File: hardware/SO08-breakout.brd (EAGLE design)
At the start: 12.4 x 20.3 mm, 3 parts, among them IC1 OPAMP-DUALU

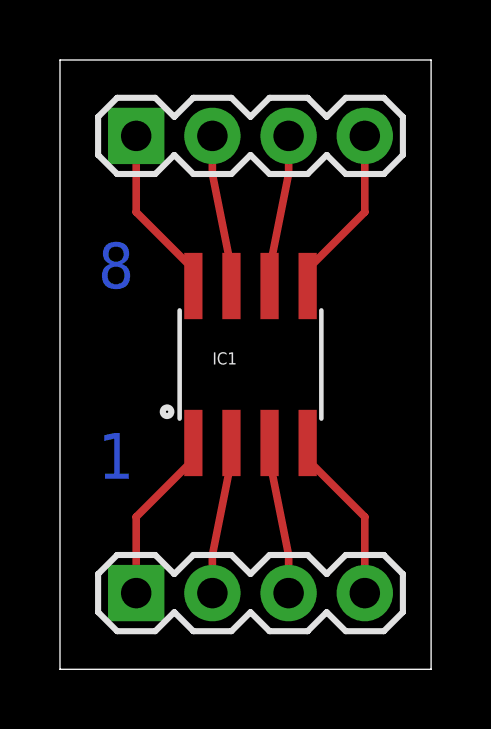
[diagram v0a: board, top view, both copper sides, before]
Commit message: made board a bit smaller
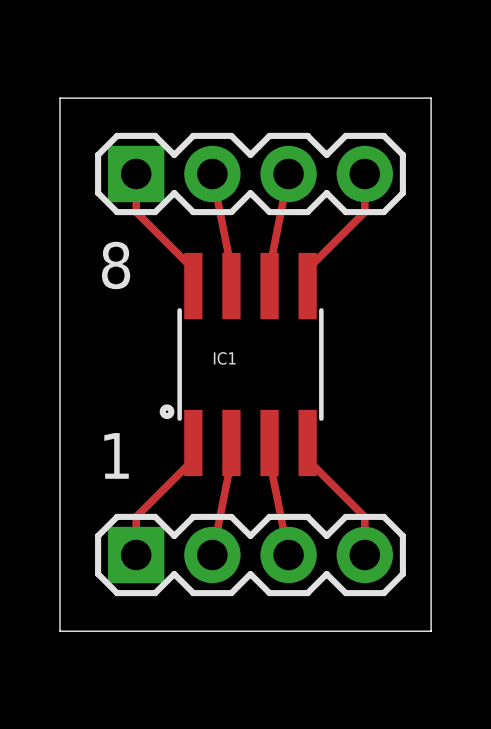
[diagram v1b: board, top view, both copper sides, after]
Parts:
- moved J1 1.27 mm to (2.54, 3.81)
- moved J2 1.27 mm to (2.54, 16.5)
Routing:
- net 3: track 5.07 -> 3.80 mm
- net 2: track 5.07 -> 3.80 mm
- net 1: track 5.79 -> 4.52 mm
- net 7: track 5.07 -> 3.80 mm
- net 6: track 5.07 -> 3.80 mm
- net 8: track 5.79 -> 4.52 mm
- net 5: track 5.79 -> 4.52 mm
- net 4: track 5.79 -> 4.52 mm
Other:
- board size 12.4 x 20.3 mm -> 12.4 x 17.8 mm
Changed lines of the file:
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@@
 <board>
 <plain>
-<wire x1="0" y1="0" x2="12.37" y2="0" width="0" layer="20"/>
-<wire x1="12.37" y1="0" x2="12.37" y2="20.31" width="0" layer="20"/>
-<wire x1="12.37" y1="20.31" x2="0" y2="20.31" width="0" layer="20"/>
-<wire x1="0" y1="20.31" x2="0" y2="0" width="0" layer="20"/>
-<text x="1.27" y="12.7" size="1.524" layer="16">8</text>
-<text x="1.27" y="6.35" size="1.524" layer="16">1</text>
+<wire x1="0" y1="1.27" x2="12.37" y2="1.27" width="0" layer="20"/>
+<wire x1="12.37" y1="1.27" x2="12.37" y2="19.04" width="0" layer="20"/>
+<wire x1="12.37" y1="19.04" x2="0" y2="19.04" width="0" layer="20"/>
+<wire x1="0" y1="19.04" x2="0" y2="1.27" width="0" layer="20"/>
+<text x="1.27" y="12.7" size="1.524" layer="121">8</text>
+<text x="1.27" y="6.35" size="1.524" layer="121">1</text>
 </plain>
 <attributes>
@@
 <elements>
 <element name="IC1" library="SparkFun-AnalogIC" package="SO08" value="OPAMP-DUALU" x="6.35" y="10.16"/>
-<element name="J1" library="SparkFun-Connectors" package="1X04" value="" x="2.54" y="2.54" smashed="yes">
-<attribute name="PROD_ID" value="CONN-09696" x="2.54" y="2.54" size="1.778" layer="27" display="off"/>
-<attribute name="VALUE" x="1.27" y="-0.635" size="1.27" layer="27"/>
+<element name="J1" library="SparkFun-Connectors" package="1X04" value="" x="2.54" y="3.81" smashed="yes">
+<attribute name="PROD_ID" value="CONN-09696" x="2.54" y="3.81" size="1.778" layer="27" display="off"/>
+<attribute name="VALUE" x="1.27" y="0.635" size="1.27" layer="27"/>
 </element>
-<element name="J2" library="SparkFun-Connectors" package="1X04" value="" x="2.54" y="17.78" smashed="yes">
-<attribute name="PROD_ID" value="CONN-09696" x="2.54" y="17.78" size="1.778" layer="27" display="off"/>
-<attribute name="VALUE" x="1.27" y="14.605" size="1.27" layer="27"/>
+<element name="J2" library="SparkFun-Connectors" package="1X04" value="" x="2.54" y="16.51" smashed="yes">
+<attribute name="PROD_ID" value="CONN-09696" x="2.54" y="16.51" size="1.778" layer="27" display="off"/>
+<attribute name="VALUE" x="1.27" y="13.335" size="1.27" layer="27"/>
 </element>
 </elements>
@@
 <contactref element="J1" pad="1"/>
 <wire x1="2.54" y1="5.08" x2="4.445" y2="6.985" width="0.254" layer="1"/>
-<wire x1="2.54" y1="2.54" x2="2.54" y2="5.08" width="0.254" layer="1"/>
+<wire x1="2.54" y1="3.81" x2="2.54" y2="5.08" width="0.254" layer="1"/>
 <wire x1="4.445" y1="6.985" x2="4.445" y2="7.5438" width="0.254" layer="1"/>
 </signal>
@@
 <contactref element="J1" pad="2"/>
 <wire x1="5.08" y1="3.81" x2="5.715" y2="6.985" width="0.254" layer="1"/>
-<wire x1="5.08" y1="2.54" x2="5.08" y2="3.81" width="0.254" layer="1"/>
 <wire x1="5.715" y1="6.985" x2="5.715" y2="7.5438" width="0.254" layer="1"/>
 </signal>
@@
 <contactref element="J1" pad="3"/>
 <wire x1="7.62" y1="3.81" x2="6.985" y2="6.985" width="0.254" layer="1"/>
-<wire x1="7.62" y1="2.54" x2="7.62" y2="3.81" width="0.254" layer="1"/>
 <wire x1="6.985" y1="6.985" x2="6.985" y2="7.5438" width="0.254" layer="1"/>
 </signal>
@@
 <contactref element="J1" pad="4"/>
 <wire x1="10.16" y1="5.08" x2="8.255" y2="6.985" width="0.254" layer="1"/>
-<wire x1="10.16" y1="2.54" x2="10.16" y2="5.08" width="0.254" layer="1"/>
+<wire x1="10.16" y1="3.81" x2="10.16" y2="5.08" width="0.254" layer="1"/>
 <wire x1="8.255" y1="6.985" x2="8.255" y2="7.5438" width="0.254" layer="1"/>
 </signal>
@@
 <contactref element="J2" pad="1"/>
 <wire x1="2.54" y1="15.24" x2="4.445" y2="13.335" width="0.254" layer="1"/>
-<wire x1="2.54" y1="17.78" x2="2.54" y2="15.24" width="0.254" layer="1"/>
+<wire x1="2.54" y1="16.51" x2="2.54" y2="15.24" width="0.254" layer="1"/>
 <wire x1="4.445" y1="13.335" x2="4.445" y2="12.7762" width="0.254" layer="1"/>
 </signal>
@@
 <contactref element="J2" pad="2"/>
 <wire x1="5.08" y1="16.51" x2="5.715" y2="13.335" width="0.254" layer="1"/>
-<wire x1="5.08" y1="17.78" x2="5.08" y2="16.51" width="0.254" layer="1"/>
 <wire x1="5.715" y1="13.335" x2="5.715" y2="12.7762" width="0.254" layer="1"/>
 </signal>
@@
 <contactref element="J2" pad="3"/>
 <wire x1="7.62" y1="16.51" x2="6.985" y2="13.335" width="0.254" layer="1"/>
-<wire x1="7.62" y1="17.78" x2="7.62" y2="16.51" width="0.254" layer="1"/>
 <wire x1="6.985" y1="13.335" x2="6.985" y2="12.7762" width="0.254" layer="1"/>
 </signal>
@@
 <contactref element="J2" pad="4"/>
 <wire x1="10.16" y1="15.24" x2="8.255" y2="13.335" width="0.254" layer="1"/>
-<wire x1="10.16" y1="17.78" x2="10.16" y2="15.24" width="0.254" layer="1"/>
+<wire x1="10.16" y1="16.51" x2="10.16" y2="15.24" width="0.254" layer="1"/>
 <wire x1="8.255" y1="13.335" x2="8.255" y2="12.7762" width="0.254" layer="1"/>
 </signal>

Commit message: - made breakout board for SO08 a bit smaller - split APRS code to APRS/AX.25/AFSK files
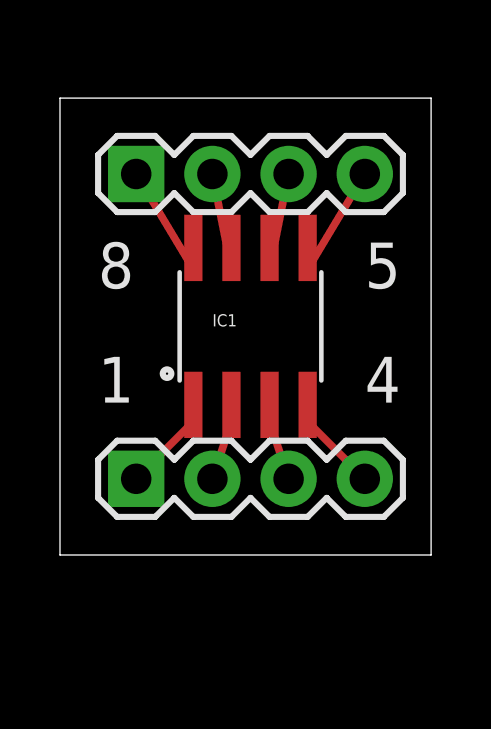
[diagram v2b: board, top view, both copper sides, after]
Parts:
- moved J1 2.54 mm to (2.54, 6.35)
- moved IC1 1.27 mm to (6.35, 11.4)
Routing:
- net 4: track 4.52 -> 3.25 mm
- net 1: track 4.52 -> 3.25 mm
- net 3: track 3.80 -> 2.57 mm
- net 2: track 3.80 -> 2.57 mm
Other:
- board size 12.4 x 17.8 mm -> 12.4 x 15.2 mm
- board text added: "4"
- board text added: "5"
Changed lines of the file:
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@@
 <board>
 <plain>
-<wire x1="0" y1="1.27" x2="12.37" y2="1.27" width="0" layer="20"/>
-<wire x1="12.37" y1="1.27" x2="12.37" y2="19.04" width="0" layer="20"/>
+<wire x1="0" y1="3.81" x2="12.37" y2="3.81" width="0" layer="20"/>
+<wire x1="12.37" y1="3.81" x2="12.37" y2="19.04" width="0" layer="20"/>
 <wire x1="12.37" y1="19.04" x2="0" y2="19.04" width="0" layer="20"/>
-<wire x1="0" y1="19.04" x2="0" y2="1.27" width="0" layer="20"/>
+<wire x1="0" y1="19.04" x2="0" y2="3.81" width="0" layer="20"/>
 <text x="1.27" y="12.7" size="1.524" layer="121">8</text>
-<text x="1.27" y="6.35" size="1.524" layer="121">1</text>
+<text x="1.27" y="8.89" size="1.524" layer="121">1</text>
+<text x="10.16" y="12.7" size="1.524" layer="121">5</text>
+<text x="10.16" y="8.89" size="1.524" layer="121">4</text>
 </plain>
 <attributes>
@@
 </autorouter>
 <elements>
-<element name="IC1" library="SparkFun-AnalogIC" package="SO08" value="OPAMP-DUALU" x="6.35" y="10.16"/>
-<element name="J1" library="SparkFun-Connectors" package="1X04" value="" x="2.54" y="3.81" smashed="yes">
-<attribute name="PROD_ID" value="CONN-09696" x="2.54" y="3.81" size="1.778" layer="27" display="off"/>
-<attribute name="VALUE" x="1.27" y="0.635" size="1.27" layer="27"/>
+<element name="IC1" library="SparkFun-AnalogIC" package="SO08" value="OPAMP-DUALU" x="6.35" y="11.43"/>
+<element name="J1" library="SparkFun-Connectors" package="1X04" value="" x="2.54" y="6.35" smashed="yes">
+<attribute name="PROD_ID" value="CONN-09696" x="2.54" y="6.35" size="1.778" layer="27" display="off"/>
+<attribute name="VALUE" x="1.27" y="3.175" size="1.27" layer="27"/>
 </element>
 <element name="J2" library="SparkFun-Connectors" package="1X04" value="" x="2.54" y="16.51" smashed="yes">
@@
 <contactref element="IC1" pad="1"/>
 <contactref element="J1" pad="1"/>
-<wire x1="2.54" y1="5.08" x2="4.445" y2="6.985" width="0.254" layer="1"/>
-<wire x1="2.54" y1="3.81" x2="2.54" y2="5.08" width="0.254" layer="1"/>
-<wire x1="4.445" y1="6.985" x2="4.445" y2="7.5438" width="0.254" layer="1"/>
+<wire x1="2.54" y1="6.35" x2="4.445" y2="8.255" width="0.254" layer="1"/>
+<wire x1="4.445" y1="8.255" x2="4.445" y2="8.8138" width="0.254" layer="1"/>
 </signal>
 <signal name="2">
 <contactref element="IC1" pad="2"/>
 <contactref element="J1" pad="2"/>
-<wire x1="5.08" y1="3.81" x2="5.715" y2="6.985" width="0.254" layer="1"/>
-<wire x1="5.715" y1="6.985" x2="5.715" y2="7.5438" width="0.254" layer="1"/>
+<wire x1="5.08" y1="6.35" x2="5.715" y2="8.255" width="0.254" layer="1"/>
+<wire x1="5.715" y1="8.255" x2="5.715" y2="8.8138" width="0.254" layer="1"/>
 </signal>
 <signal name="3">
 <contactref element="IC1" pad="3"/>
 <contactref element="J1" pad="3"/>
-<wire x1="7.62" y1="3.81" x2="6.985" y2="6.985" width="0.254" layer="1"/>
-<wire x1="6.985" y1="6.985" x2="6.985" y2="7.5438" width="0.254" layer="1"/>
+<wire x1="7.62" y1="6.35" x2="6.985" y2="8.255" width="0.254" layer="1"/>
+<wire x1="6.985" y1="8.255" x2="6.985" y2="8.8138" width="0.254" layer="1"/>
 </signal>
 <signal name="4">
 <contactref element="IC1" pad="4"/>
 <contactref element="J1" pad="4"/>
-<wire x1="10.16" y1="5.08" x2="8.255" y2="6.985" width="0.254" layer="1"/>
-<wire x1="10.16" y1="3.81" x2="10.16" y2="5.08" width="0.254" layer="1"/>
-<wire x1="8.255" y1="6.985" x2="8.255" y2="7.5438" width="0.254" layer="1"/>
+<wire x1="10.16" y1="6.35" x2="8.255" y2="8.255" width="0.254" layer="1"/>
+<wire x1="8.255" y1="8.255" x2="8.255" y2="8.8138" width="0.254" layer="1"/>
 </signal>
 <signal name="8">
 <contactref element="IC1" pad="8"/>
 <contactref element="J2" pad="1"/>
-<wire x1="2.54" y1="15.24" x2="4.445" y2="13.335" width="0.254" layer="1"/>
-<wire x1="2.54" y1="16.51" x2="2.54" y2="15.24" width="0.254" layer="1"/>
-<wire x1="4.445" y1="13.335" x2="4.445" y2="12.7762" width="0.254" layer="1"/>
+<wire x1="2.54" y1="16.51" x2="4.445" y2="13.335" width="0.254" layer="1"/>
+<wire x1="4.445" y1="13.335" x2="4.445" y2="14.0462" width="0.254" layer="1"/>
 </signal>
 <signal name="7">
@@
 <contactref element="J2" pad="2"/>
 <wire x1="5.08" y1="16.51" x2="5.715" y2="13.335" width="0.254" layer="1"/>
-<wire x1="5.715" y1="13.335" x2="5.715" y2="12.7762" width="0.254" layer="1"/>
+<wire x1="5.715" y1="13.335" x2="5.715" y2="14.0462" width="0.254" layer="1"/>
 </signal>
 <signal name="6">
@@
 <contactref element="J2" pad="3"/>
 <wire x1="7.62" y1="16.51" x2="6.985" y2="13.335" width="0.254" layer="1"/>
-<wire x1="6.985" y1="13.335" x2="6.985" y2="12.7762" width="0.254" layer="1"/>
+<wire x1="6.985" y1="13.335" x2="6.985" y2="14.0462" width="0.254" layer="1"/>
 </signal>
 <signal name="5">
 <contactref element="IC1" pad="5"/>
 <contactref element="J2" pad="4"/>
-<wire x1="10.16" y1="15.24" x2="8.255" y2="13.335" width="0.254" layer="1"/>
-<wire x1="10.16" y1="16.51" x2="10.16" y2="15.24" width="0.254" layer="1"/>
-<wire x1="8.255" y1="13.335" x2="8.255" y2="12.7762" width="0.254" layer="1"/>
+<wire x1="10.16" y1="16.51" x2="8.255" y2="13.335" width="0.254" layer="1"/>
+<wire x1="8.255" y1="13.335" x2="8.255" y2="14.0462" width="0.254" layer="1"/>
 </signal>
 </signals>
